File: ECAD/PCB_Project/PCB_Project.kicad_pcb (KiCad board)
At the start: 2 copper layers, 105.4 x 113 mm, 2 parts

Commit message: First PCB Draft
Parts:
- added C201: 1uF, Capacitor_THT:C_Disc_D4.3mm_W1.9mm_P5.00mm, F.Cu at (129.2, 159.2)
- added C202: 1uF, Capacitor_THT:C_Disc_D4.3mm_W1.9mm_P5.00mm, F.Cu at (101.3, 159.4)
- added C203: 1uF, Capacitor_THT:C_Disc_D4.3mm_W1.9mm_P5.00mm, F.Cu at (103.8, 159.4)
- added C204: 1uF, Capacitor_THT:C_Disc_D4.3mm_W1.9mm_P5.00mm, F.Cu at (106.3, 159.4)
- added C205: 1uF, Capacitor_THT:C_Disc_D4.3mm_W1.9mm_P5.00mm, F.Cu at (108.9, 159.4)
- added C206: 1uF, Capacitor_THT:C_Disc_D4.3mm_W1.9mm_P5.00mm, F.Cu at (111.4, 159.4)
- added C207: 1uF, Capacitor_THT:C_Disc_D4.3mm_W1.9mm_P5.00mm, F.Cu at (116.5, 159.4)
- added C208: 1uF, Capacitor_THT:C_Disc_D4.3mm_W1.9mm_P5.00mm, F.Cu at (121.6, 164.2)
- added C209: 1uF, Capacitor_THT:C_Disc_D4.3mm_W1.9mm_P5.00mm, F.Cu at (126.7, 164.2)
- added C301: 1uF, Capacitor_THT:C_Disc_D4.3mm_W1.9mm_P5.00mm, F.Cu at (128.6, 73.3)
- added C302: 100uF, Capacitor_THT:C_Disc_D4.3mm_W1.9mm_P5.00mm, F.Cu at (128.6, 77.2)
- added C303: 100nF, Capacitor_THT:C_Disc_D4.3mm_W1.9mm_P5.00mm, F.Cu at (123.5, 73.3)
- added C304: 100nF, Capacitor_THT:C_Disc_D4.3mm_W1.9mm_P5.00mm, F.Cu at (162.2, 73.4)
- added J301: Conn_01x03, Connector_PinHeader_2.54mm:PinHeader_1x03_P2.54mm_Vertical, F.Cu at (93.0, 86.7)
- added J302: Conn_01x04, Connector_PinHeader_2.54mm:PinHeader_1x04_P2.54mm_Vertical, F.Cu at (157.2, 79.7)
- added J303: Conn_01x02, Connector_PinHeader_2.54mm:PinHeader_1x02_P2.54mm_Vertical, F.Cu at (94.3, 70.2)
- added J304: Conn_01x04, Connector_PinHeader_2.54mm:PinHeader_1x04_P2.54mm_Vertical, F.Cu at (133.7, 83.5)
- added J305: Conn_01x03, Connector_PinHeader_2.54mm:PinHeader_1x03_P2.54mm_Vertical, F.Cu at (143.2, 70.8)
- added J401: Conn_01x10, Connector_PinSocket_2.54mm:PinSocket_1x10_P2.54mm_Vertical, B.Cu at (102.5, 70.8)
- added J402: Conn_01x10, Connector_PinSocket_2.54mm:PinSocket_1x10_P2.54mm_Vertical, B.Cu at (148.3, 70.8)
- added J403: Conn_01x02, Connector_PinHeader_2.54mm:PinHeader_1x02_P2.54mm_Vertical, B.Cu at (105.1, 70.8)
- added Q301: NPN, Package_TO_SOT_THT:TO-92S_Wide, F.Cu at (87.9, 73.1)
- added R301: 100k, Resistor_THT:R_Axial_DIN0204_L3.6mm_D1.6mm_P7.62mm_Horizontal, F.Cu at (90.5, 83.5)
- added R302: R, Resistor_THT:R_Axial_DIN0204_L3.6mm_D1.6mm_P7.62mm_Horizontal, F.Cu at (89.2, 67.0)
- added R303: 10k, Resistor_THT:R_Axial_DIN0204_L3.6mm_D1.6mm_P7.62mm_Horizontal, F.Cu at (96.2, 83.5)
- added R304: 10k, Resistor_THT:R_Axial_DIN0204_L3.6mm_D1.6mm_P7.62mm_Horizontal, F.Cu at (93.7, 83.5)
- moved U201 53.7 mm to (125.4, 161.1)
- moved U301 53.5 mm to (124.8, 97.5), turned to 180 degrees
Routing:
- net +3V3: track 0.00 -> 266.0 mm, vias 0 -> 2
- net /Display/DISPLAY.SDI: track 0.00 -> 121.9 mm, vias 0 -> 1
- net /Display/DISPLAY.SCL: track 0.00 -> 99.5 mm, vias 0 -> 1
- net /Display/DISPLAY.A0: track 0.00 -> 97.5 mm, vias 0 -> 1
- net +12V: track 0.00 -> 78.1 mm, vias 0 -> 1
- net /Display/DISPLAY.NRST: track 0.00 -> 74.2 mm, vias 0 -> 1
- net /Display/DISPLAY.NCS: track 0.00 -> 73.2 mm, vias 0 -> 1
- net GND: track 0.00 -> 49.3 mm, vias 0 -> 5
- net +5V: track 0.00 -> 40.2 mm, vias 0 -> 1
- net /MCU/Driver.DIR: track 0.00 -> 24.9 mm, vias 0 -> 1
- net Net-(U201-CAP1N): track 0.00 -> 14.1 mm
- net /MCU/LDR_Analog: track 0.00 -> 11.7 mm, vias 0 -> 1
- net /MCU/Driver.MS2: track 0.00 -> 11.4 mm, vias 0 -> 1
- net Net-(U201-CAP2P): track 0.00 -> 10.6 mm
- net Net-(J304-Pin_3): track 0.00 -> 10.2 mm
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- added copper zone on B.Cu, net GND
- added copper zone on F.Cu, net GND
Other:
- board size 105.4 x 113 mm -> 80 x 100 mm
- board text added: "DISPLAY"
- board text added: "DRIVER"
- board text added: "IND"
- board text added: "SG90"
- board text added: "STEP"
- board text added: "US"

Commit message: PCB Update
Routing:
- net +3V3: track 266.0 -> 266.7 mm
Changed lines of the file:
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@@
   (setup
     (stackup
-      (layer "F.SilkS" (type "Top Silk Screen"))
+      (layer "dielectric 1" (type "Top Silk Screen") (thickness 0) (material "FR4") (epsilon_r 4.5) (loss_tangent 0.02))
       (layer "F.Paste" (type "Top Solder Paste"))
       (layer "F.Mask" (type "Top Solder Mask") (thickness 0.01))
       (layer "F.Cu" (type "copper") (thickness 0.035))
-      (layer "dielectric 1" (type "core") (thickness 1.51) (material "FR4") (epsilon_r 4.5) (loss_tangent 0.02))
+      (layer "dielectric 2" (type "core") (thickness 1.51) (material "FR4") (epsilon_r 4.5) (loss_tangent 0.02))
       (layer "B.Cu" (type "copper") (thickness 0.035))
       (layer "B.Mask" (type "Bottom Solder Mask") (thickness 0.01))
       (layer "B.Paste" (type "Bottom Solder Paste"))
-      (layer "B.SilkS" (type "Bottom Silk Screen"))
+      (layer "dielectric 3" (type "Bottom Silk Screen") (thickness 0) (material "FR4") (epsilon_r 4.5) (loss_tangent 0.02))
       (copper_finish "None")
       (dielectric_constraints no)
@@
     )
   )
-  (gr_rect locked (start 86.03 165.71) (end 166.03 65.71)
+  (gr_rect locked (start 86.03 65.71) (end 166.03 165.71)
     (stroke (width 0.1) (type default)) (fill none) (layer "Edge.Cuts"))
-  (gr_text "STEP" (at 134.29 100 90) (layer "F.Cu")
+  (gr_text "STEP" (at 135.56 100 90) (layer "F.Cu")
     (effects (font (size 1.5 1.5) (thickness 0.3) bold) (justify left bottom))
   )
@@
   (segment (start 162.23 73.37) (end 160.92 72.06) (width 1.5) (layer "B.Cu") (net 16))
   (segment (start 110.076598 71.976598) (end 110.076598 68.25) (width 1.5) (layer "B.Cu") (net 16))
-  (segment (start 98.73 79.68) (end 99.156877 79.253123) (width 1.5) (layer "B.Cu") (net 16))
+  (segment (start 87.9 73.095) (end 87.9 77.778846) (width 1.5) (layer "B.Cu") (net 16))
   (segment (start 116.51 78.41) (end 110.076598 71.976598) (width 1.5) (layer "B.Cu") (net 16))
   (segment (start 123.495 93.65) (end 119.05 93.65) (width 1.5) (layer "B.Cu") (net 16))
@@
   (segment (start 87.9 68.285) (end 87.9 73.095) (width 1.5) (layer "B.Cu") (net 16))
   (segment (start 160.92 72.06) (end 157.15 72.06) (width 1.5) (layer "B.Cu") (net 16))
+  (segment (start 99.156877 71.823123) (end 100.19 70.79) (width 1.5) (layer "B.Cu") (net 16))
   (segment (start 136.83 154.7625) (end 136.83 152.07) (width 1.5) (layer "B.Cu") (net 16))
   (segment (start 116.51 91.11) (end 110.795 91.11) (width 1.5) (layer "B.Cu") (net 16))
   (segment (start 136.83 152.07) (end 135.56 150.8) (width 1.5) (layer "B.Cu") (net 16))
-  (segment (start 99.156877 71.823123) (end 100.19 70.79) (width 1.5) (layer "B.Cu") (net 16))
+  (segment (start 87.9 77.778846) (end 89.801154 79.68) (width 1.5) (layer "B.Cu") (net 16))
   (segment (start 110.076598 68.25) (end 102.54 68.25) (width 1.5) (layer "B.Cu") (net 16))
-  (segment (start 100.19 70.79) (end 102.54 70.79) (width 1.5) (layer "B.Cu") (net 16))
   (segment (start 99.156877 79.253123) (end 99.156877 71.823123) (width 1.5) (layer "B.Cu") (net 16))
-  (segment (start 91.032309 79.68) (end 98.73 79.68) (width 1.5) (layer "B.Cu") (net 16))
-  (segment (start 87.9 76.547691) (end 91.032309 79.68) (width 1.5) (layer "B.Cu") (net 16))
-  (segment (start 87.9 73.095) (end 87.9 76.547691) (width 1.5) (layer "B.Cu") (net 16))
+  (segment (start 98.73 79.68) (end 99.156877 79.253123) (width 1.5) (layer "B.Cu") (net 16))
   (segment (start 134.29 152.07) (end 134.29 154.7625) (width 1.5) (layer "B.Cu") (net 16))
   (segment (start 89.205 66.98) (end 87.9 68.285) (width 1.5) (layer "B.Cu") (net 16))
   (segment (start 119.05 93.65) (end 116.51 91.11) (width 1.5) (layer "B.Cu") (net 16))
+  (segment (start 89.801154 79.68) (end 98.73 79.68) (width 1.5) (layer "B.Cu") (net 16))
   (segment (start 152.31 67.22) (end 111.106598 67.22) (width 1.5) (layer "B.Cu") (net 16))
   (segment (start 111.106598 67.22) (end 110.076598 68.25) (width 1.5) (layer "B.Cu") (net 16))
   (segment (start 116.51 91.11) (end 116.51 78.41) (width 1.5) (layer "B.Cu") (net 16))
+  (segment (start 100.19 70.79) (end 102.54 70.79) (width 1.5) (layer "B.Cu") (net 16))
   (segment (start 157.15 72.06) (end 152.31 67.22) (width 1.5) (layer "B.Cu") (net 16))
   (segment (start 153.34 83.49) (end 148.26 83.49) (width 1.5) (layer "F.Cu") (net 17))

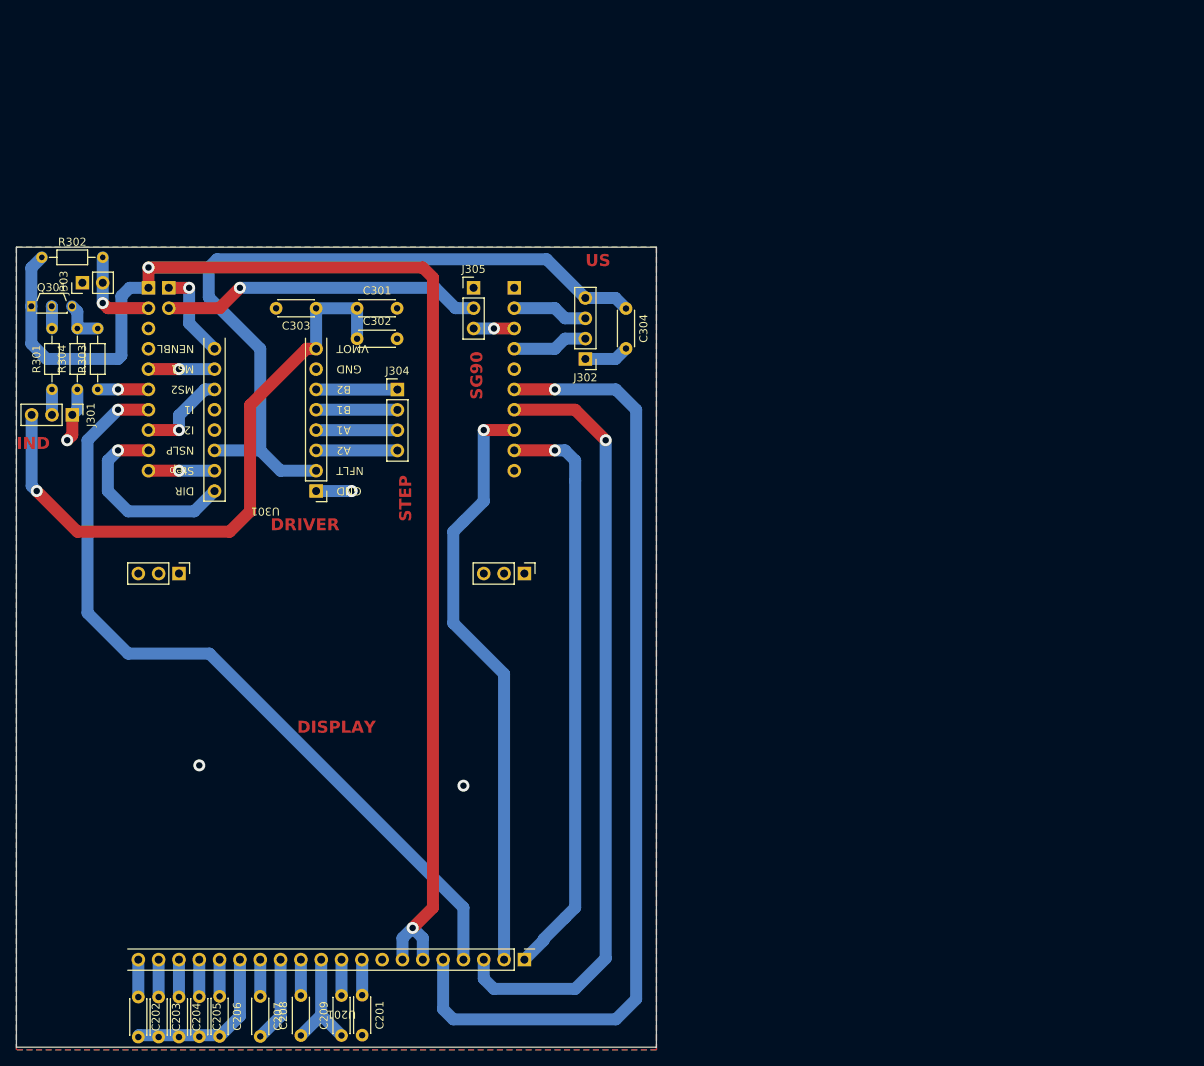
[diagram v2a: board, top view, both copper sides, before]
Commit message: PCB Overhaul
Stripboard Expansion
-created
-schematic
-routing

Main PCB
-Flipped sides to not cover buttons
-Started Rerouting
-Changed schematic to accomodate stripboard expansion
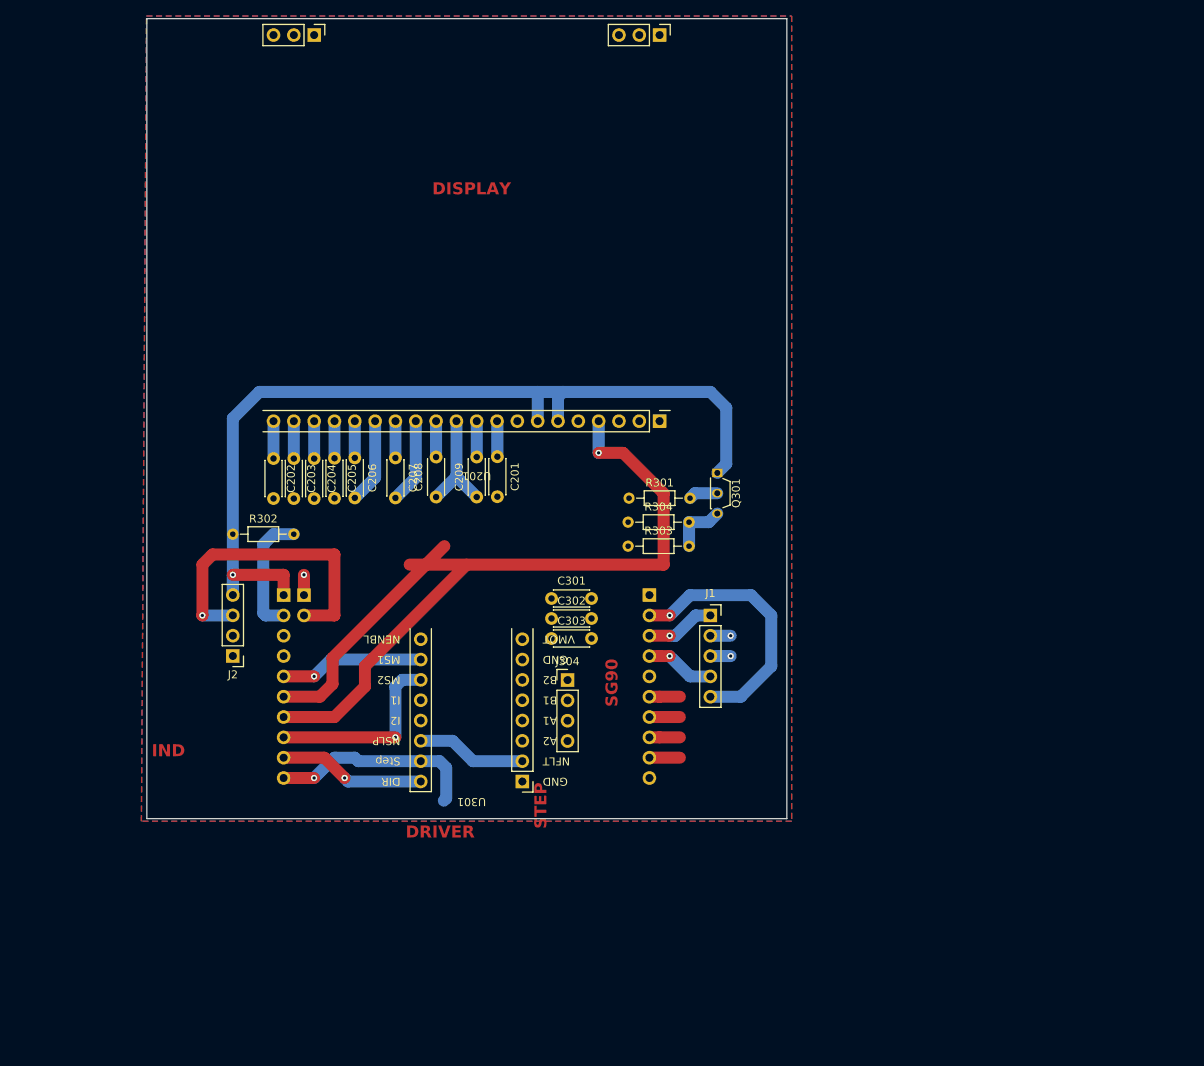
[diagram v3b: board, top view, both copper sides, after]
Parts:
- removed C304: 100nF, Capacitor_THT:C_Disc_D4.3mm_W1.9mm_P5.00mm
- removed J301, J305: Conn_01x03, Connector_PinHeader_2.54mm:PinHeader_1x03_P2.54mm_Vertical
- removed J302: Conn_01x04, Connector_PinHeader_2.54mm:PinHeader_1x04_P2.54mm_Vertical
- removed J303: Conn_01x02, Connector_PinHeader_2.54mm:PinHeader_1x02_P2.54mm_Vertical
- added J1: DIST_MCU, Connector_PinSocket_2.54mm:PinSocket_1x05_P2.54mm_Vertical, F.Cu at (172.8, 111.7)
- added J2: DIST_Power, Connector_PinHeader_2.54mm:PinHeader_1x04_P2.54mm_Vertical, F.Cu at (113.1, 116.8)
- moved Q301 88.2 mm to (173.6, 93.9), turned to -90 degrees
- moved R301 73.4 mm to (162.6, 97.1), turned to 0 degrees
- moved R304 70.8 mm to (162.5, 100.1), turned to 0 degrees
- moved C201 69.4 mm to (146.2, 91.9)
- moved C206 69.4 mm to (128.3, 92.0)
- moved C207 69.4 mm to (133.4, 92.0)
- moved U201 69.4 mm to (142.3, 93.8)
- moved C202 69.4 mm to (118.2, 92.1)
- moved C203 69.4 mm to (120.7, 92.1)
- moved C204 69.4 mm to (123.2, 92.1)
- moved C205 69.4 mm to (125.8, 92.1)
- moved C208 69.4 mm to (138.5, 96.9)
- moved C209 69.4 mm to (143.6, 96.9)
- moved R303 69.1 mm to (162.5, 103.1), turned to 0 degrees
- moved C303 50.7 mm to (152.9, 114.6), turned to 0 degrees
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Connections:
- R301 pad 1: Net-(J301-Pin_2) -> /Sensors + Motor/Inductive_12V
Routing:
- net +3V3: track 266.7 -> 127.3 mm, vias 2 -> 1
- net /Display/DISPLAY.SDI: track 121.9 -> 3.81 mm, vias 1 -> 0
- net /Display/DISPLAY.A0: track 97.5 -> 3.81 mm, vias 1 -> 0
- net +12V: track 78.1 -> 0.00 mm, vias 1 -> 0
- net /Display/DISPLAY.NRST: track 74.2 -> 3.81 mm, vias 1 -> 0
- net /Display/DISPLAY.NCS: track 73.2 -> 3.81 mm, vias 1 -> 0
- net GND: track 49.3 -> 13.2 mm, vias 5 -> 1
- net /MCU/Ultrasonic.Trigg: track 9.42 -> 32.9 mm, vias 0 -> 1
- net /MCU/Ind_Analog: track 6.35 -> 29.8 mm, vias 1 -> 0
- net /MCU/Driver.STEP: track 8.25 -> 26.1 mm
- net /Display/DISPLAY.SCL: track 99.5 -> 87.1 mm
- net /MCU/Driver.MS2: track 11.4 -> 23.8 mm
- net Net-(J304-Pin_3): track 10.2 -> 0.00 mm
- net Net-(J304-Pin_1): track 10.2 -> 0.00 mm
- net Net-(J304-Pin_4): track 10.2 -> 0.00 mm
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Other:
- board text removed: "US"

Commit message: Final PCB
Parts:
- removed U301: ~, 318_Footprint_Library:MP6500
- added J3: 12V, TerminalBlock:TerminalBlock_bornier-2_P5.08mm, F.Cu at (154.4, 133.3)
- added JP1: Jumper_2_Open, Resistor_SMD:R_1206_3216Metric, B.Cu at (144.8, 106.7)
- added JP2: Jumper_2_Open, Resistor_SMD:R_1206_3216Metric, B.Cu at (148.1, 106.7)
- added U1: ~, 318_Footprint_Library:MP6500, F.Cu at (132.2, 127.0)
- J304: value Conn_01x04 -> STEPPER; footprint Connector_PinHeader_2.54mm:PinHeader_1x04_P2.54mm_Vertical -> TerminalBlock:TerminalBlock_bornier-4_P5.08mm
- R301, R303, R304: footprint Resistor_THT:R_Axial_DIN0204_L3.6mm_D1.6mm_P7.62mm_Horizontal -> Resistor_SMD:R_1206_3216Metric; moved to B.Cu
- R302: footprint Resistor_THT:R_Axial_DIN0204_L3.6mm_D1.6mm_P7.62mm_Horizontal -> Resistor_SMD:R_1206_3216Metric
- moved J304 15.2 mm to (148.1, 133.3), turned to 180 degrees
- moved C302 12.5 mm to (154.4, 124.5)
- moved C303 12.5 mm to (154.4, 127.0)
- moved C301 12.3 mm to (154.4, 121.9), turned to 90 degrees
- moved J1 10.2 mm to (172.8, 121.9), turned to 180 degrees
- moved R302 9.46 mm to (116.3, 110.5), turned to -90 degrees
- moved R303 7.84 mm to (170.3, 101.9)
- moved R304 7.81 mm to (170.2, 99.0)
- moved R301 7.77 mm to (170.3, 96.0)
- moved J2 1.86 mm to (111.2, 116.8)
- moved Q301 1.27 mm to (174.9, 93.9)
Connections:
- C301 pad 2: GND -> /Sensors + Motor/MGND
- C302 pad 2: GND -> /Sensors + Motor/MGND
- C303 pad 2: GND -> /Sensors + Motor/MGND
- J1 pad 1: /MCU/P1.6/I_O! -> /MCU/LDR_Analog
- J1 pad 2: /MCU/LDR_Analog -> /Sensors + Motor/Inductive_12V
- J1 pad 3: /Sensors + Motor/Inductive_12V -> /MCU/Ultrasonic.Echo
- J1 pad 4: /MCU/Ultrasonic.Echo -> /MCU/P1.6/I_O!
- J401 pad 5: /MCU/Driver.MS1 -> /MCU/P2.7/I_O!
- J401 pad 8: /MCU/Driver.MS2 -> /MCU/P2.5/I_O!
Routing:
- net +12V: track 0.00 -> 89.7 mm, vias 0 -> 2
- net /MCU/LDR_Analog: track 18.1 -> 95.9 mm
- net /Display/DISPLAY.NCS: track 3.81 -> 67.8 mm, vias 0 -> 1
- net /Display/DISPLAY.NRST: track 3.81 -> 58.7 mm, vias 0 -> 1
- net /Sensors + Motor/Inductive_12V: track 2.54 -> 47.6 mm, vias 1 -> 0
- net /Display/DISPLAY.A0: track 3.81 -> 40.9 mm, vias 0 -> 1
- net /Sensors + Motor/MGND: track 0.00 -> 35.5 mm
- net /Display/DISPLAY.SDI: track 3.81 -> 39.2 mm, vias 0 -> 1
- net /MCU/Ind_Analog: track 29.8 -> 60.8 mm, vias 0 -> 1
- net +3V3: track 127.3 -> 101.4 mm, vias 1 -> 2
- net /MCU/Ultrasonic.Trigg: track 32.9 -> 7.62 mm
- net /MCU/Driver.MS2: track 23.8 -> 0.00 mm, vias 1 -> 0
- net /MCU/Driver.MS1: track 18.0 -> 0.00 mm, vias 1 -> 0
- net Net-(J304-Pin_4): track 0.00 -> 9.99 mm
- net Net-(J304-Pin_3): track 0.00 -> 8.93 mm
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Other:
- board text removed: "DRIVER"
- board text removed: "IND"
- board text removed: "SG90"
- board text removed: "STEP"
